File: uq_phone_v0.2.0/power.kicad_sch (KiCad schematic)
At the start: 37 parts, among them J2 124018312112A, J3 BM03B-ACHSS-GAN-TF_LF__SN_, U1 TPS62162DSGR, U15 TPS22964CYZPR, U2 MCP73871-2CCI_ML, U3 BQ27441DRZR-G1A

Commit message: Regulator EN-controlled soft power latch prototype
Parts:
- added C24: 100nF, Capacitor_SMD:C_0201_0603Metric, symbol Capacitors:capacitor_100nF
- added D12, D2: BAT54, symbol BAT54:Diode-NC_pin
- added Q4: BSS84, Package_TO_SOT_SMD:SOT-23, symbol Transistor_FET:BSS84
- added Q5: MMBT3904LP-7, MMBT3904LP-7:DFN101X61X53-3N, symbol MMBT3904LP-7:MMBT3904LP-7
- added R30, R34: 100k, Resistor_SMD:R_0201_0603Metric, symbol Resistors:Resistor_100k
- added R31: 47k, Resistor_SMD:R_0201_0603Metric, symbol Resistors:Resistor_47k
- added R32: 4.7k, Resistor_SMD:R_0201_0603Metric, symbol Resistors:Resistor_4k7
- added R35: 10k, Resistor_SMD:R_0201_0603Metric, symbol Resistors:Resistor_10k
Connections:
- net +3.3V: now also R35.2
- net GND: now also Q5.2, R31.1, R34.2
- net MCP_OUT: now also C24.1, Q4.2 (S), R30.2; no longer U1.3 (EN)
- new net: Q5.1, R31.2, R32.1
- new net PWR_BUTTON_RAW: D12.2 (C), D2.2 (C)
- new net PWR_BUTTON_SENSE: D12.1 (A), R35.1
- new net PWR_HOLD: R32.2
- new net Q1_GATE: C24.2, D2.1 (A), Q4.1 (G), Q5.3, R30.1
- new net SYSTEM_EN: Q4.3 (D), R34.1, U1.3 (EN)
- no-connect marks 14 -> 15
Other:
- moved on the sheet: B1, C1, C30, C31, TP1, TP2, TP3, TP5, TP6, U15

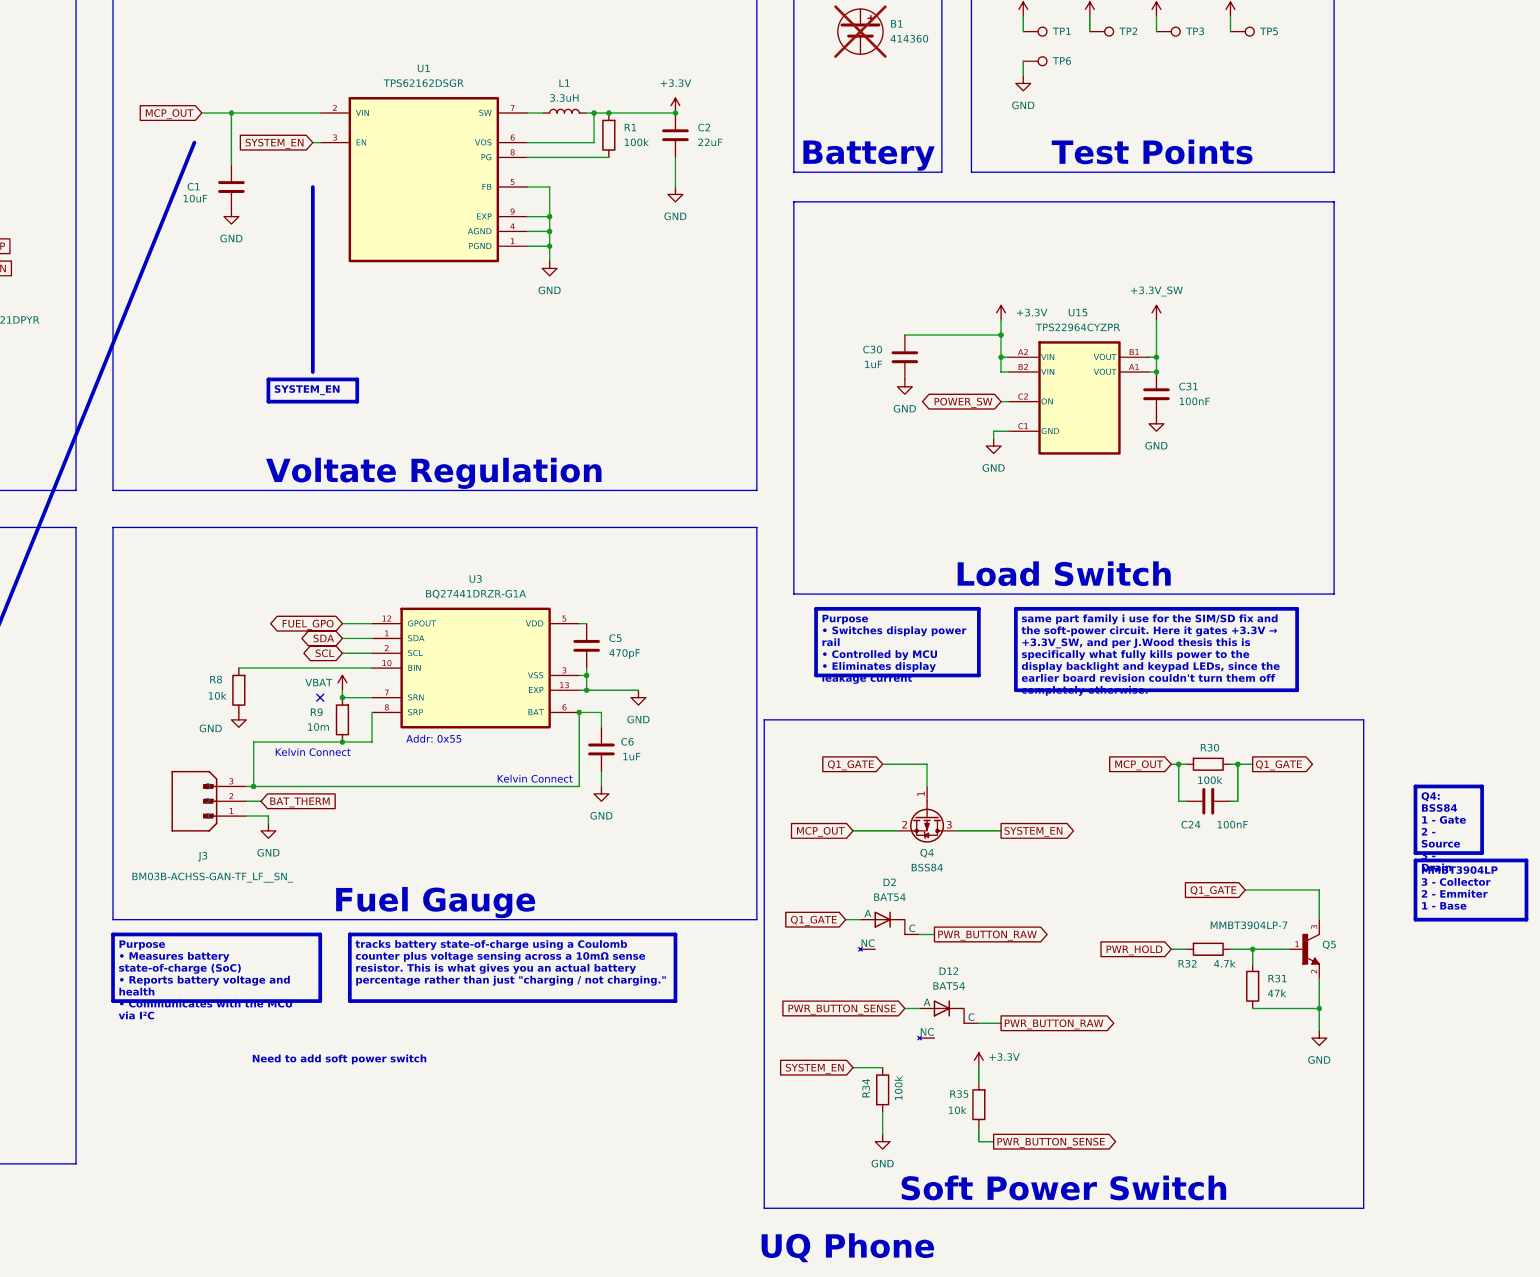
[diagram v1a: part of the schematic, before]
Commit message: VIN Based Latching circuit - switch off power to reg
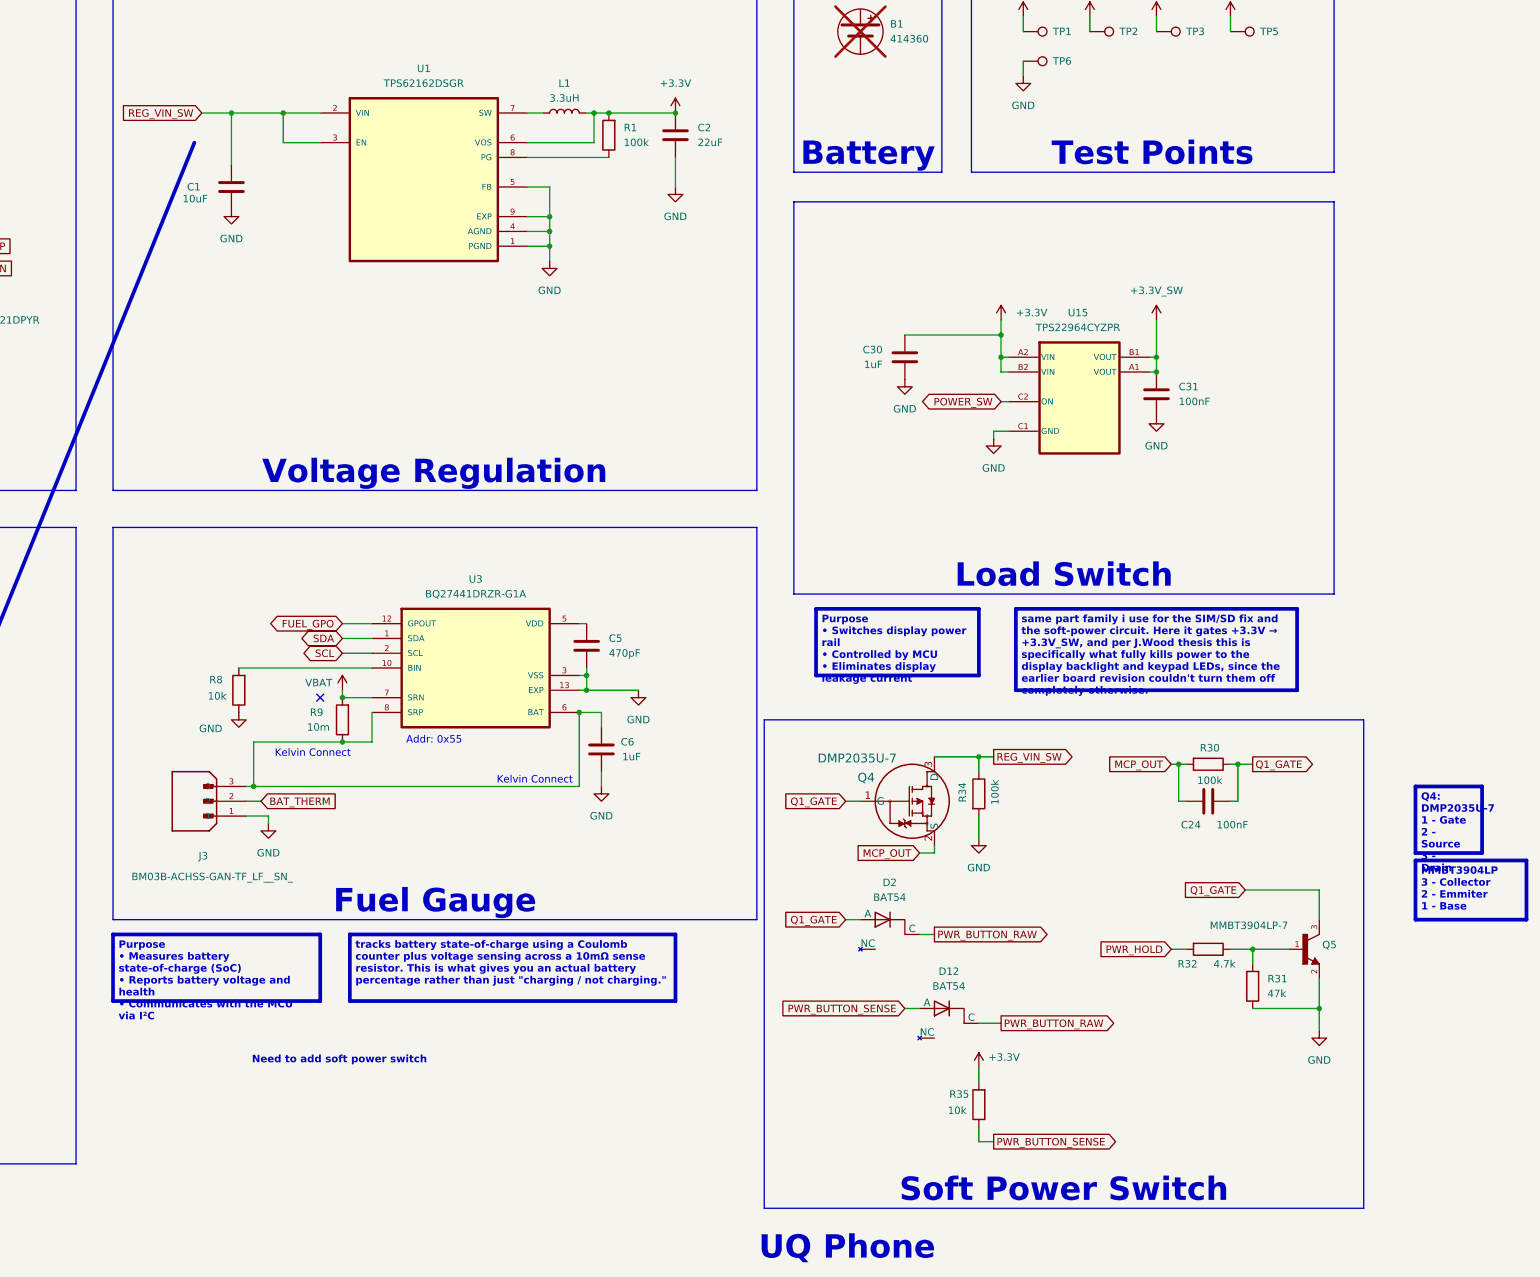
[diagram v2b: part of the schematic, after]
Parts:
- removed Q4: BSS84, Package_TO_SOT_SMD:SOT-23, symbol Transistor_FET:BSS84
- added Q4: DMP2035U-7, SOT23_DIO, symbol DMP2035U-7:DMP2035U-7
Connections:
- net MCP_OUT: now also Q4.2 (S); no longer C1.2, U1.2 (VIN)
- net Q1_GATE: now also Q4.1 (G)
- net SYSTEM_EN renamed REG_VIN_SW
- net REG_VIN_SW: now also C1.2, U1.2 (VIN), Q4.3 (D)

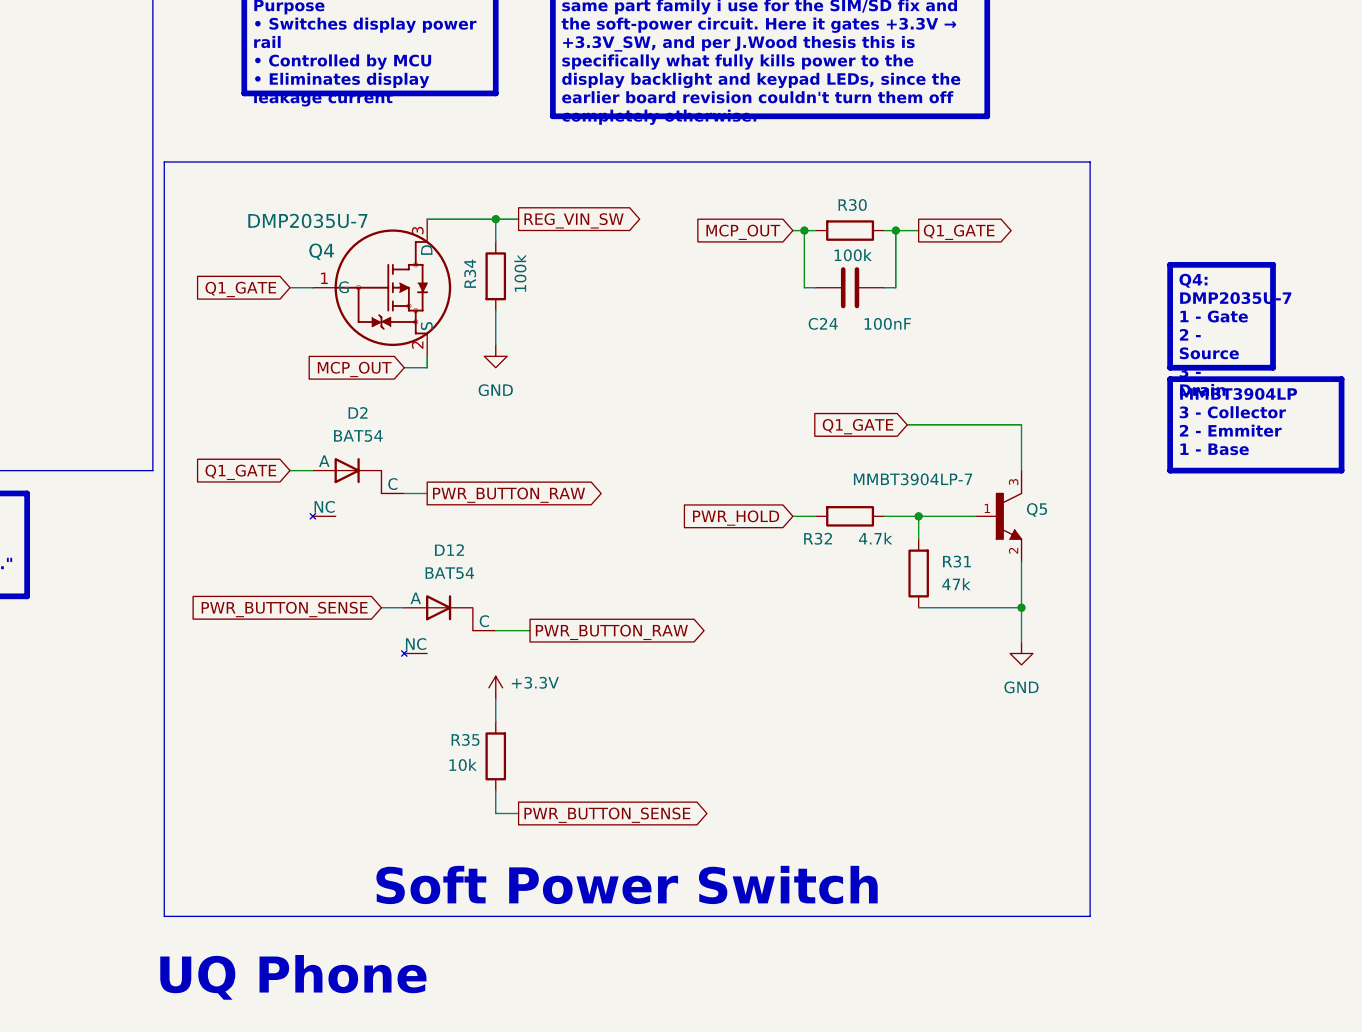
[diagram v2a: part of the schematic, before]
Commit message: Add soft power switch and update PCB design
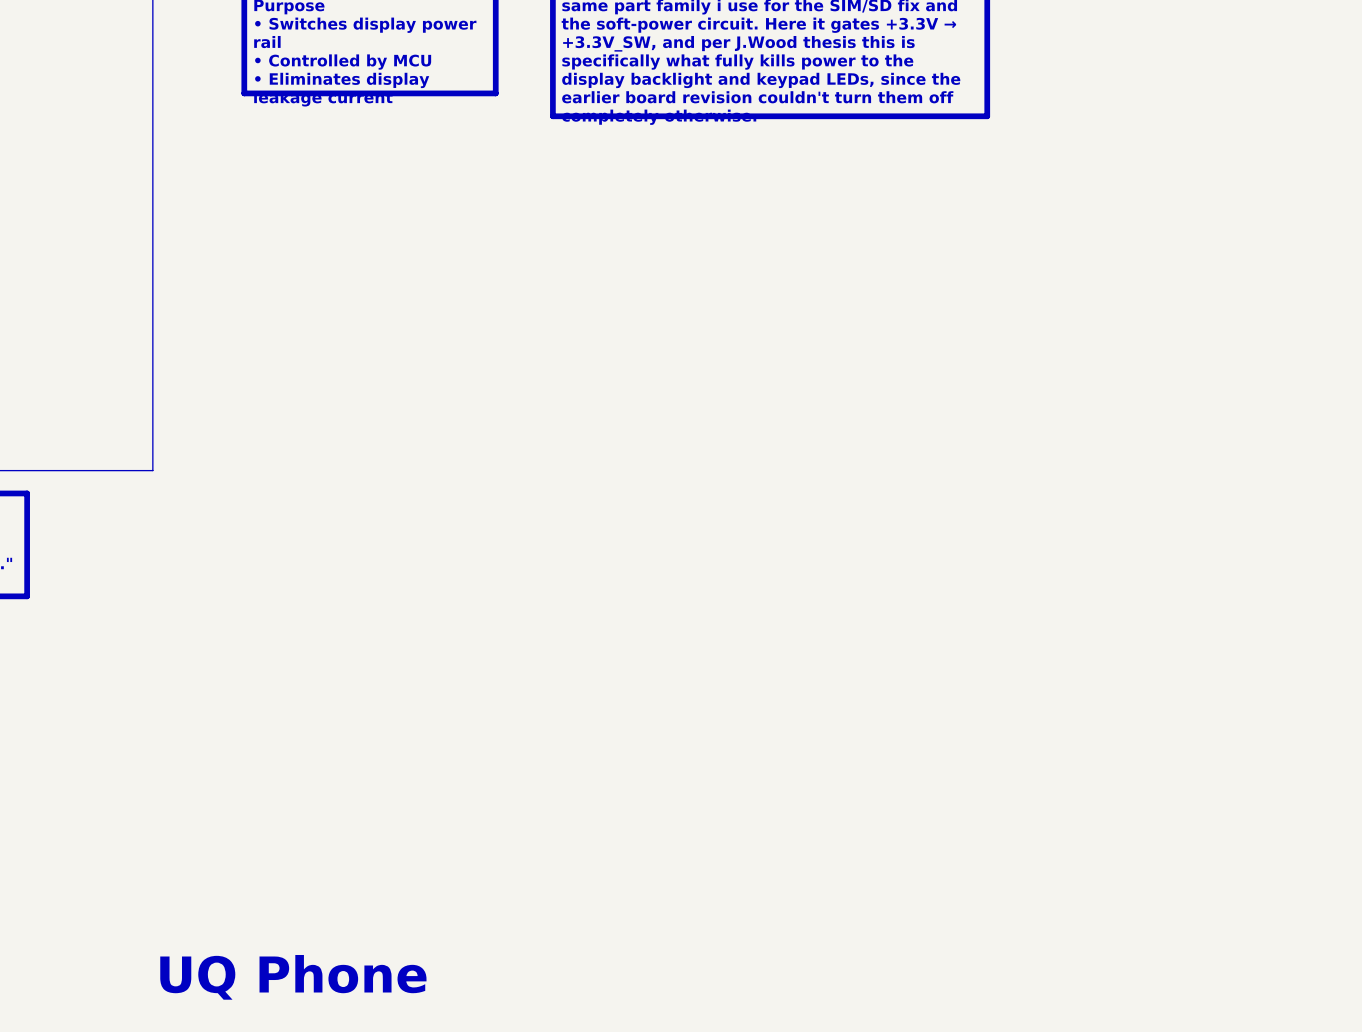
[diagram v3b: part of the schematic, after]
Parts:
- removed C24: 100nF, Capacitor_SMD:C_0201_0603Metric, symbol Capacitors:capacitor_100nF
- removed D12, D2: BAT54, symbol BAT54:Diode-NC_pin
- removed Q4: DMP2035U-7, SOT23_DIO, symbol DMP2035U-7:DMP2035U-7
- removed Q5: MMBT3904LP-7, MMBT3904LP-7:DFN101X61X53-3N, symbol MMBT3904LP-7:MMBT3904LP-7
- removed R30, R34: 100k, Resistor_SMD:R_0201_0603Metric, symbol Resistors:Resistor_100k
- removed R31: 47k, Resistor_SMD:R_0201_0603Metric, symbol Resistors:Resistor_47k
- removed R32: 4.7k, Resistor_SMD:R_0201_0603Metric, symbol Resistors:Resistor_4k7
- removed R35: 10k, Resistor_SMD:R_0201_0603Metric, symbol Resistors:Resistor_10k

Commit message: Fix KiCad libraries and update soft power circuit
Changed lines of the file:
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@@
 	(text_box "USB-C Connector\n• External power input (VBUS)\n• USB 2.0 data interface\n• Supplies VUSB to battery manager\n• CC resistors configure USB2.0 device mode"
 		(exclude_from_sim no)
-		(at 90.17 16.51 0)
+		(at 95.25 16.51 0)
 		(size 55.88 11.43)
 		(margins 0.9525 0.9525 0.9525 0.9525)

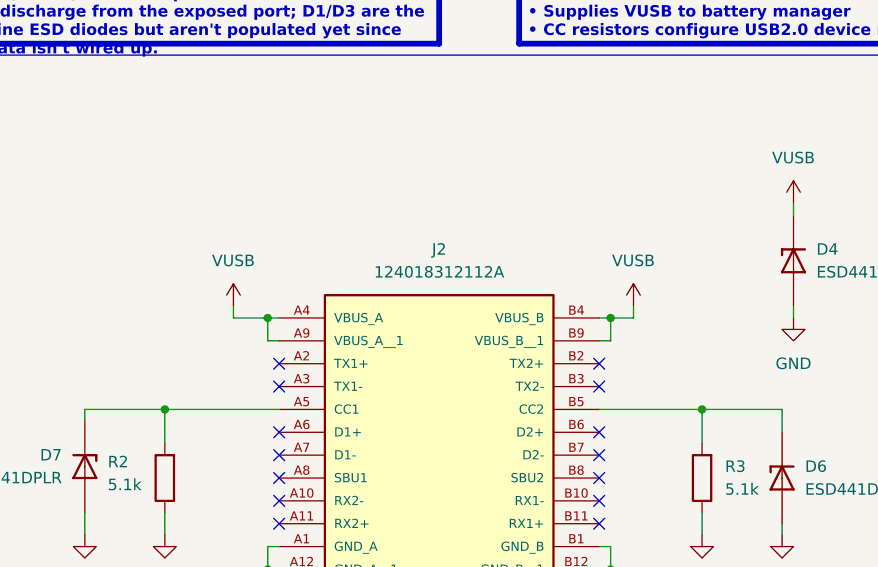
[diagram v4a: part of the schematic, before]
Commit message: Complete STM32H723ZGI6 144-pin schematic and FMC mapping
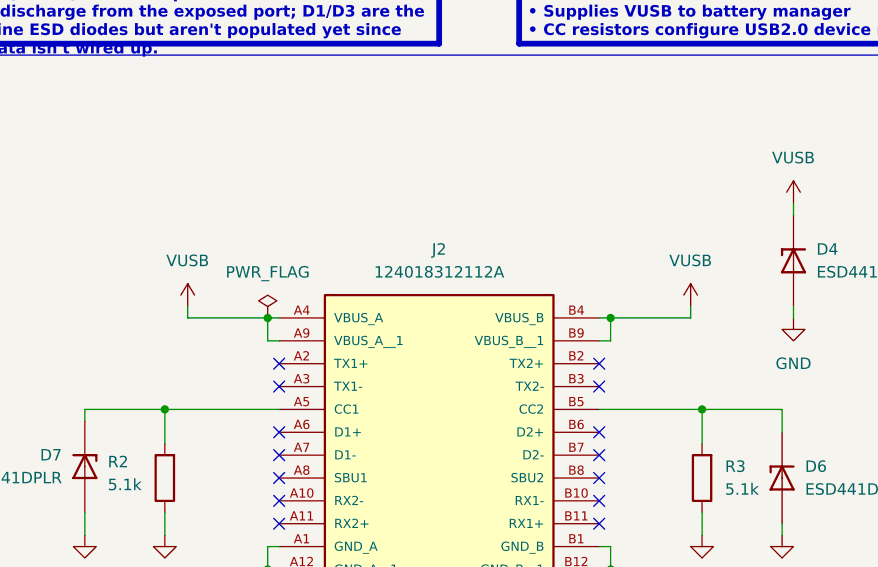
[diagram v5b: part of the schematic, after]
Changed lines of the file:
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@@
 	(wire
 		(pts
-			(xy 107.95 58.42) (xy 107.95 57.15)
+			(xy 114.3 58.42) (xy 114.3 57.15)
 		)
 		(stroke
@@
 	(wire
 		(pts
-			(xy 63.5 58.42) (xy 67.31 58.42)
+			(xy 58.42 58.42) (xy 67.31 58.42)
 		)
 		(stroke
@@
 	(wire
 		(pts
-			(xy 107.95 58.42) (xy 105.41 58.42)
+			(xy 114.3 58.42) (xy 105.41 58.42)
 		)
 		(stroke
@@
 	(wire
 		(pts
-			(xy 63.5 57.15) (xy 63.5 58.42)
+			(xy 58.42 57.15) (xy 58.42 58.42)
 		)
 		(stroke
@@
 	)
 	(symbol
+		(lib_id "power:PWR_FLAG")
+		(at 67.31 58.42 0)
+		(unit 1)
+		(exclude_from_sim no)
+		(in_bom yes)
+		(on_board yes)
+		(dnp no)
+		(fields_autoplaced yes)
+		(property "Reference" "#FLG01"
+			(at 67.31 56.515 0)
+			(effects
+				(font
+					(size 1.27 1.27)
+				)
+				(hide yes)
+			)
+		)
+		(property "Value" "PWR_FLAG"
+			(at 67.31 53.34 0)
+			(effects
+				(font
+					(size 1.27 1.27)
+				)
+			)
+		)
+		(property "Footprint" ""
+			(at 67.31 58.42 0)
+			(effects
+				(font
+					(size 1.27 1.27)
+				)
+				(hide yes)
+			)
+		)
+		(property "Datasheet" "~"
+			(at 67.31 58.42 0)
+			(effects
+				(font
+					(size 1.27 1.27)
+				)
+				(hide yes)
+			)
+		)
+		(property "Description" "Special symbol for telling ERC where power comes from"
+			(at 67.31 58.42 0)
+			(effects
+				(font
+					(size 1.27 1.27)
+				)
+				(hide yes)
+			)
+		)
+		(pin "1"
+		)
+		(instances
+			(project ""
+				(path "/14f57415-6807-40a5-bb38-3cb818a2cdae/e697a7f0-03cd-4a38-a369-080a37468a6a"
+					(reference "#FLG01")
+					(unit 1)
+				)
+			)
+		)
+	)
+	(symbol
 		(lib_id "power:VBUS")
 		(at 346.71 46.99 0)
@@
 	(symbol
 		(lib_id "power:VCC")
-		(at 107.95 57.15 0)
+		(at 114.3 57.15 0)
 		(unit 1)
 		(exclude_from_sim no)
@@
 		(fields_autoplaced yes)
 		(property "Reference" "#PWR07"
-			(at 107.95 60.96 0)
+			(at 114.3 60.96 0)
 			(effects
 				(font
@@
 		)
 		(property "Value" "VUSB"
-			(at 107.95 52.07 0)
+			(at 114.3 52.07 0)
 			(effects
 				(font
@@
 		)
 		(property "Footprint" ""
-			(at 107.95 57.15 0)
+			(at 114.3 57.15 0)
 			(effects
 				(font
@@
 		)
 		(property "Datasheet" ""
-			(at 107.95 57.15 0)
+			(at 114.3 57.15 0)
 			(effects
 				(font
@@
 		)
 		(property "Description" "Power symbol creates a global label with name \"VCC\""
-			(at 107.95 57.15 0)
+			(at 114.3 57.15 0)
 			(effects
 				(font
@@
 	(symbol
 		(lib_id "power:VCC")
-		(at 63.5 57.15 0)
+		(at 58.42 57.15 0)
 		(unit 1)
 		(exclude_from_sim no)
@@
 		(fields_autoplaced yes)
 		(property "Reference" "#PWR06"
-			(at 63.5 60.96 0)
+			(at 58.42 60.96 0)
 			(effects
 				(font
@@
 		)
 		(property "Value" "VUSB"
-			(at 63.5 52.07 0)
+			(at 58.42 52.07 0)
 			(effects
 				(font
@@
 		)
 		(property "Footprint" ""
-			(at 63.5 57.15 0)
+			(at 58.42 57.15 0)
 			(effects
 				(font
@@
 		)
 		(property "Datasheet" ""
-			(at 63.5 57.15 0)
+			(at 58.42 57.15 0)
 			(effects
 				(font
@@
 		)
 		(property "Description" "Power symbol creates a global label with name \"VCC\""
-			(at 63.5 57.15 0)
+			(at 58.42 57.15 0)
 			(effects
 				(font
